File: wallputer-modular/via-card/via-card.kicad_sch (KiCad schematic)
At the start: 1 part

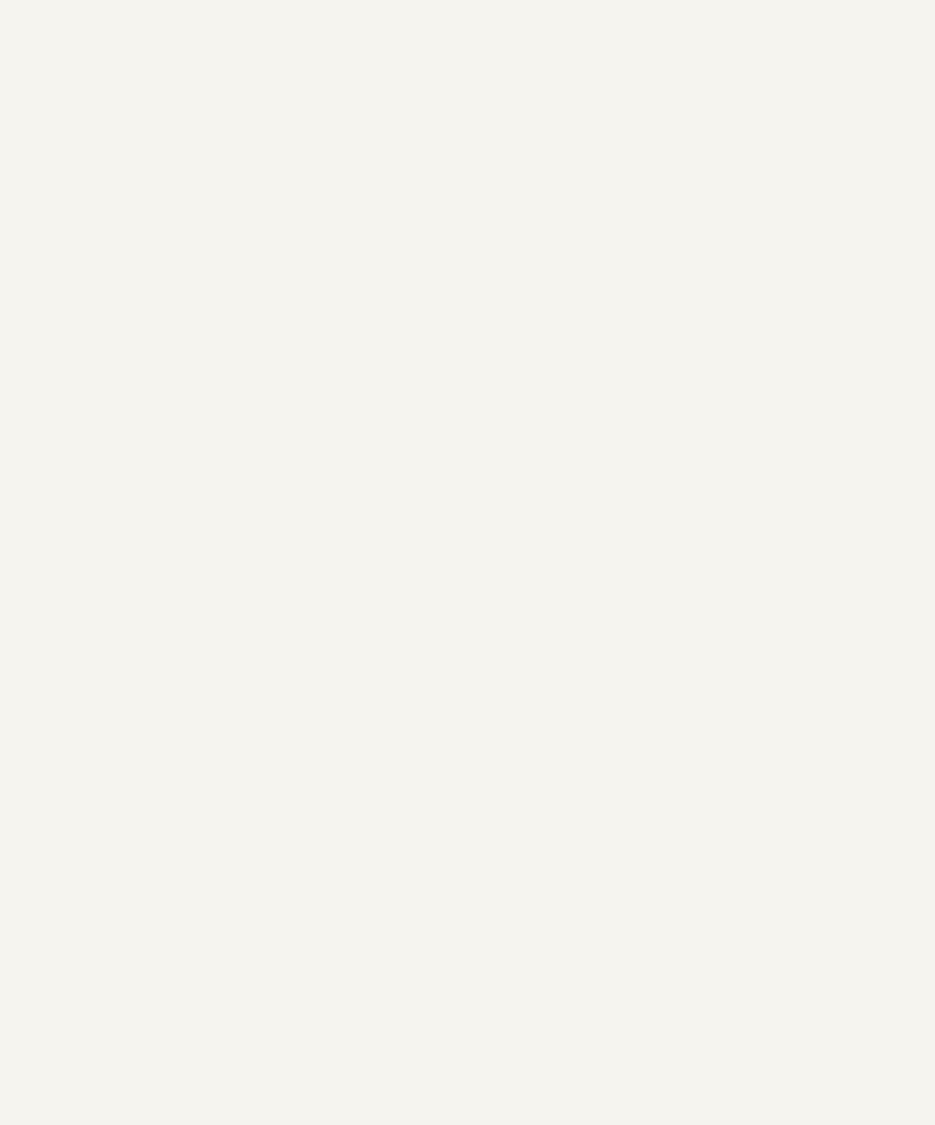
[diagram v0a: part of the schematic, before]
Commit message: copy parts of single board
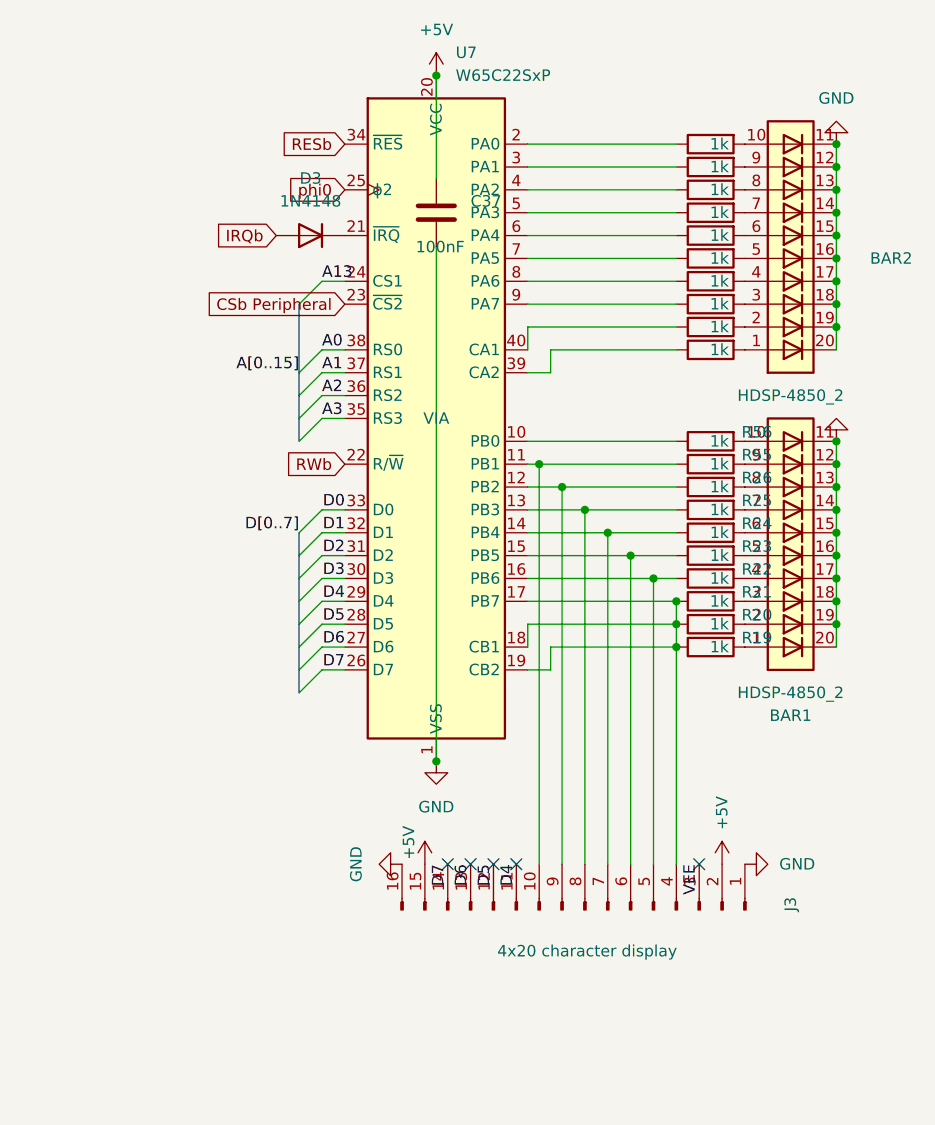
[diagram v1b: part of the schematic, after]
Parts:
- added BAR1, BAR2: HDSP-4850_2, Display:HDSP-4850, symbol LED:HDSP-4850_2
- added C37: 100nF, Capacitor_THT:C_Disc_D5.0mm_W2.5mm_P5.00mm, symbol Device:C
- added D3: 1N4148, Diode_THT:D_DO-35_SOD27_P7.62mm_Horizontal, symbol Diode:1N4148
- added J3: 4x20 character display, Connector_PinHeader_2.54mm:PinHeader_1x16_P2.54mm_Vertical, symbol Connector:Conn_01x16_Pin
- added R19, R20, R21, R22, R23, R24, R25, R26, R51, R52, R55, R56, R57, R58, R59, R60, R61, R62, R63, R64: 1k, Resistor_THT:R_Axial_DIN0204_L3.6mm_D1.6mm_P2.54mm_Vertical, symbol Device:R
- added U7: W65C22SxP, Package_DIP:DIP-40_W15.24mm, symbol 65xx-library:W65C22SxP
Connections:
- net +5V: now also C37.1, J3.15 (Pin_15), J3.2 (Pin_2), U7.20 (VCC)
- net GND: now also BAR1.11 (K), BAR1.12 (K), BAR1.13 (K), BAR1.14 (K), BAR1.15 (K), BAR1.16 (K), BAR1.17 (K), BAR1.18 (K), BAR1.19 (K), BAR1.20 (K), BAR2.11 (K), BAR2.12 (K), BAR2.13 (K), BAR2.14 (K), BAR2.15 (K), BAR2.16 (K), BAR2.17 (K), BAR2.18 (K), BAR2.19 (K), BAR2.20 (K), C37.2, J3.1 (Pin_1), J3.16 (Pin_16), U7.1 (VSS)
- new net: J3.6 (Pin_6), R23.1, U7.15 (PB5)
- new net: BAR1.5 (A), R23.2
- new net: R52.1, U7.3 (PA1)
- new net: BAR2.9 (A), R52.2
- new net: J3.4 (Pin_4), R19.1, R20.1, R21.1, U7.17 (PB7), U7.18 (CB1), U7.19 (CB2)
- new net: BAR1.2 (A), R20.2
- new net: R51.1, U7.2 (PA0)
- new net: BAR2.10 (A), R51.2
- new net: BAR2.1 (A), R59.2
- new net: BAR2.2 (A), R60.2
- new net: BAR2.3 (A), R61.2
- new net: BAR2.4 (A), R62.2
- new net: BAR2.5 (A), R63.2
- new net: BAR2.6 (A), R64.2
- new net: BAR2.7 (A), R58.2
- new net: BAR2.8 (A), R57.2
- new net: R60.1, U7.40 (CA1)
- new net: R63.1, U7.7 (PA5)
- new net: D3.1 (K), U7.21 (~{IRQ})
- new net: J3.9 (Pin_9), R26.1, U7.12 (PB2)
- new net: BAR1.8 (A), R26.2
- new net: J3.10 (Pin_10), R55.1, U7.11 (PB1)
- new net: BAR1.9 (A), R55.2
- new net: R57.1, U7.4 (PA2)
- new net: BAR1.1 (A), R19.2
- new net: R62.1, U7.8 (PA6)
- new net: BAR1.10 (A), R56.2
- new net: BAR1.3 (A), R21.2
- new net: BAR1.4 (A), R22.2
- new net: BAR1.6 (A), R24.2
- new net: BAR1.7 (A), R25.2
- new net: J3.5 (Pin_5), R22.1, U7.16 (PB6)
- new net: R59.1, U7.39 (CA2)
- new net: R61.1, U7.9 (PA7)
- new net: J3.7 (Pin_7), R24.1, U7.14 (PB4)
- new net: J3.8 (Pin_8), R25.1, U7.13 (PB3)
- new net: R64.1, U7.6 (PA4)
- new net: R56.1, U7.10 (PB0)
- new net: R58.1, U7.5 (PA3)
- new net A0: U7.38 (RS0)
- new net A1: U7.37 (RS1)
- new net A13: U7.24 (CS1)
- new net A2: U7.36 (RS2)
- new net A3: U7.35 (RS3)
- new net CSb Peripheral: U7.23 (~{CS2})
- new net D0: U7.33 (D0)
- new net D1: U7.32 (D1)
- new net D2: U7.31 (D2)
- new net D3: U7.30 (D3)
- new net D4: J3.11 (Pin_11), U7.29 (D4)
- new net D5: J3.12 (Pin_12), U7.28 (D5)
- new net D6: J3.13 (Pin_13), U7.27 (D6)
- new net D7: J3.14 (Pin_14), U7.26 (D7)
- new net IRQb: D3.2 (A)
- new net RESb: U7.34 (~{RES})
- new net RWb: U7.22 (R/~{W})
- new net VEE: J3.3 (Pin_3)
- new net phi0: U7.25 (ϕ2)
- no-connect marks 0 -> 5

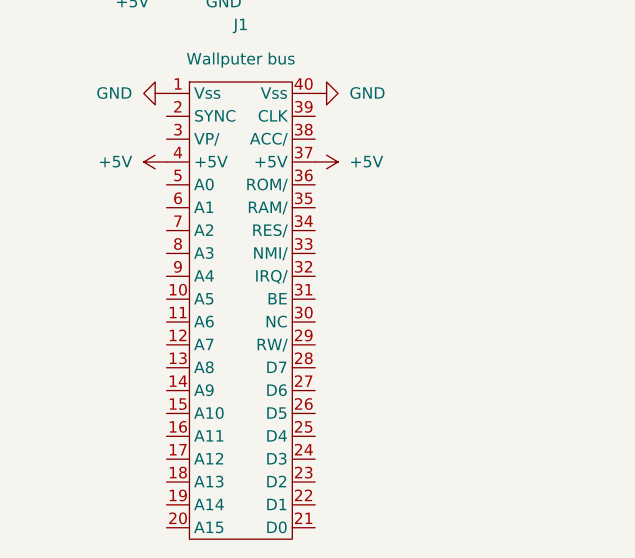
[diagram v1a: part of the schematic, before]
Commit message: implement acia card
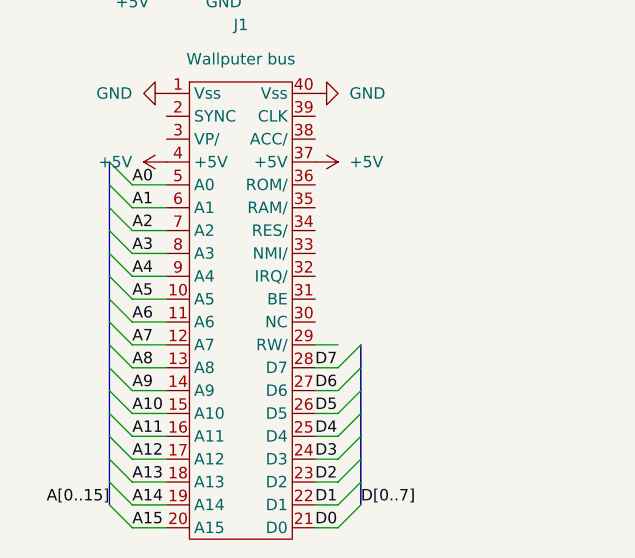
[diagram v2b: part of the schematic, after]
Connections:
- net A0: now also J1.5 (A0)
- net A1: now also J1.6 (A1)
- net A13: now also J1.18 (A13)
- net A2: now also J1.7 (A2)
- net A3: now also J1.8 (A3)
- net D0: now also J1.21 (D0)
- net D1: now also J1.22 (D1)
- net D2: now also J1.23 (D2)
- net D3: now also J1.24 (D3)
- net D4: now also J1.25 (D4)
- net D5: now also J1.26 (D5)
- net D6: now also J1.27 (D6)
- net D7: now also J1.28 (D7)
- net A5: now reaches J1.10 (A5)
- net A6: now reaches J1.11 (A6)
- net A7: now reaches J1.12 (A7)
- net A8: now reaches J1.13 (A8)
- net A9: now reaches J1.14 (A9)
- net A10: now reaches J1.15 (A10)
- net A11: now reaches J1.16 (A11)
- net A12: now reaches J1.17 (A12)
- net A14: now reaches J1.19 (A14)
- net A15: now reaches J1.20 (A15)
- net A4: now reaches J1.9 (A4)

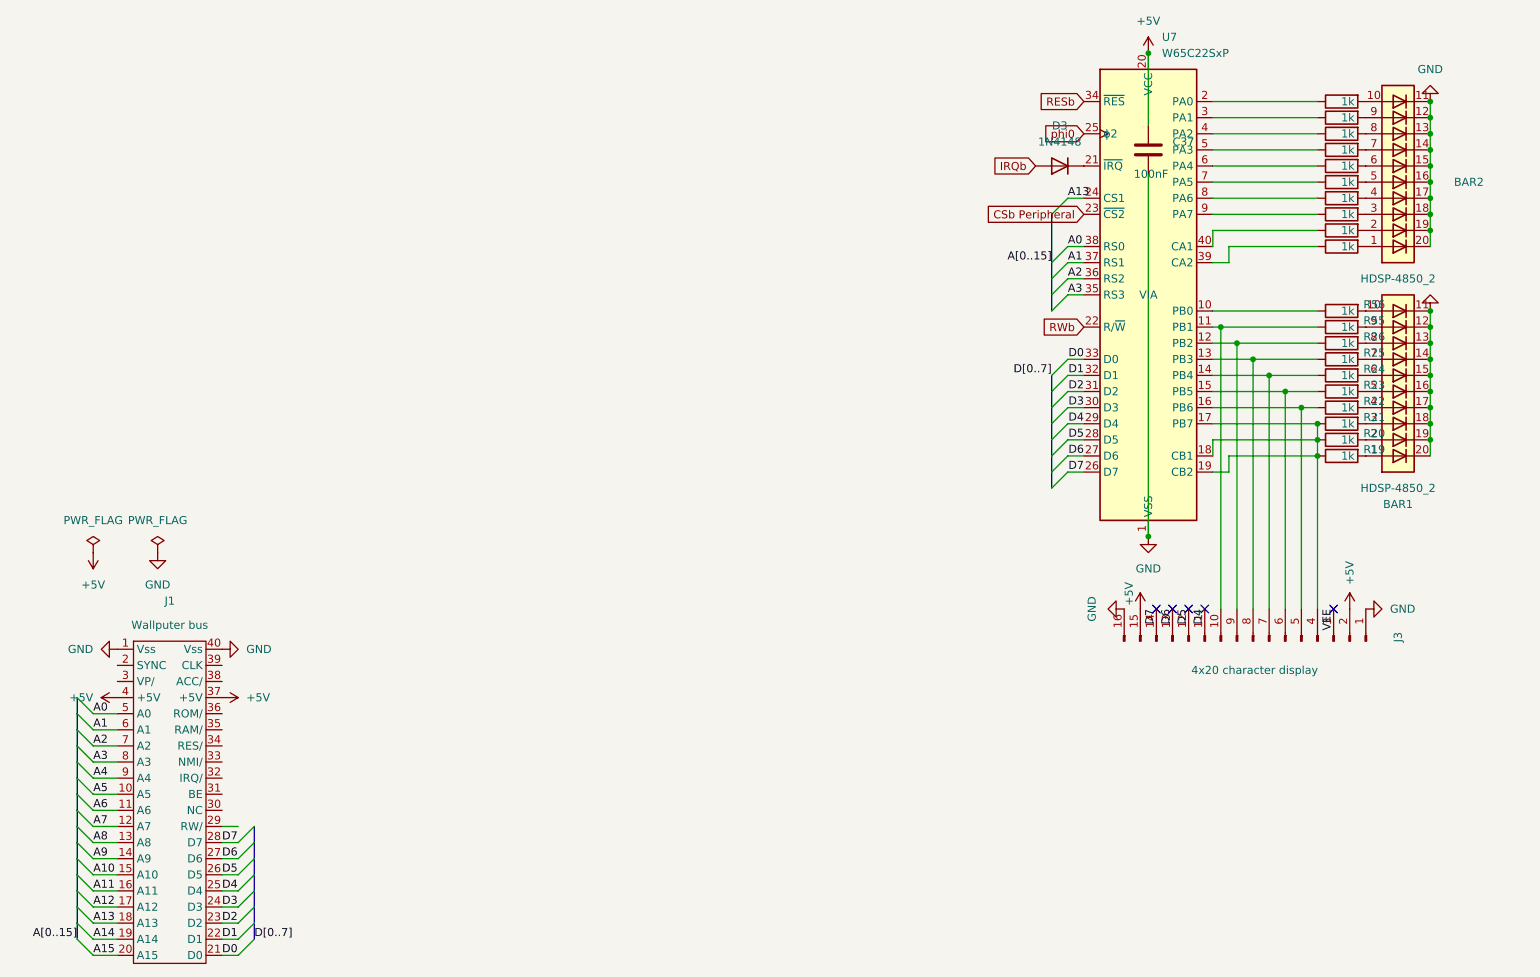
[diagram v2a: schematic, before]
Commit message: implement via board
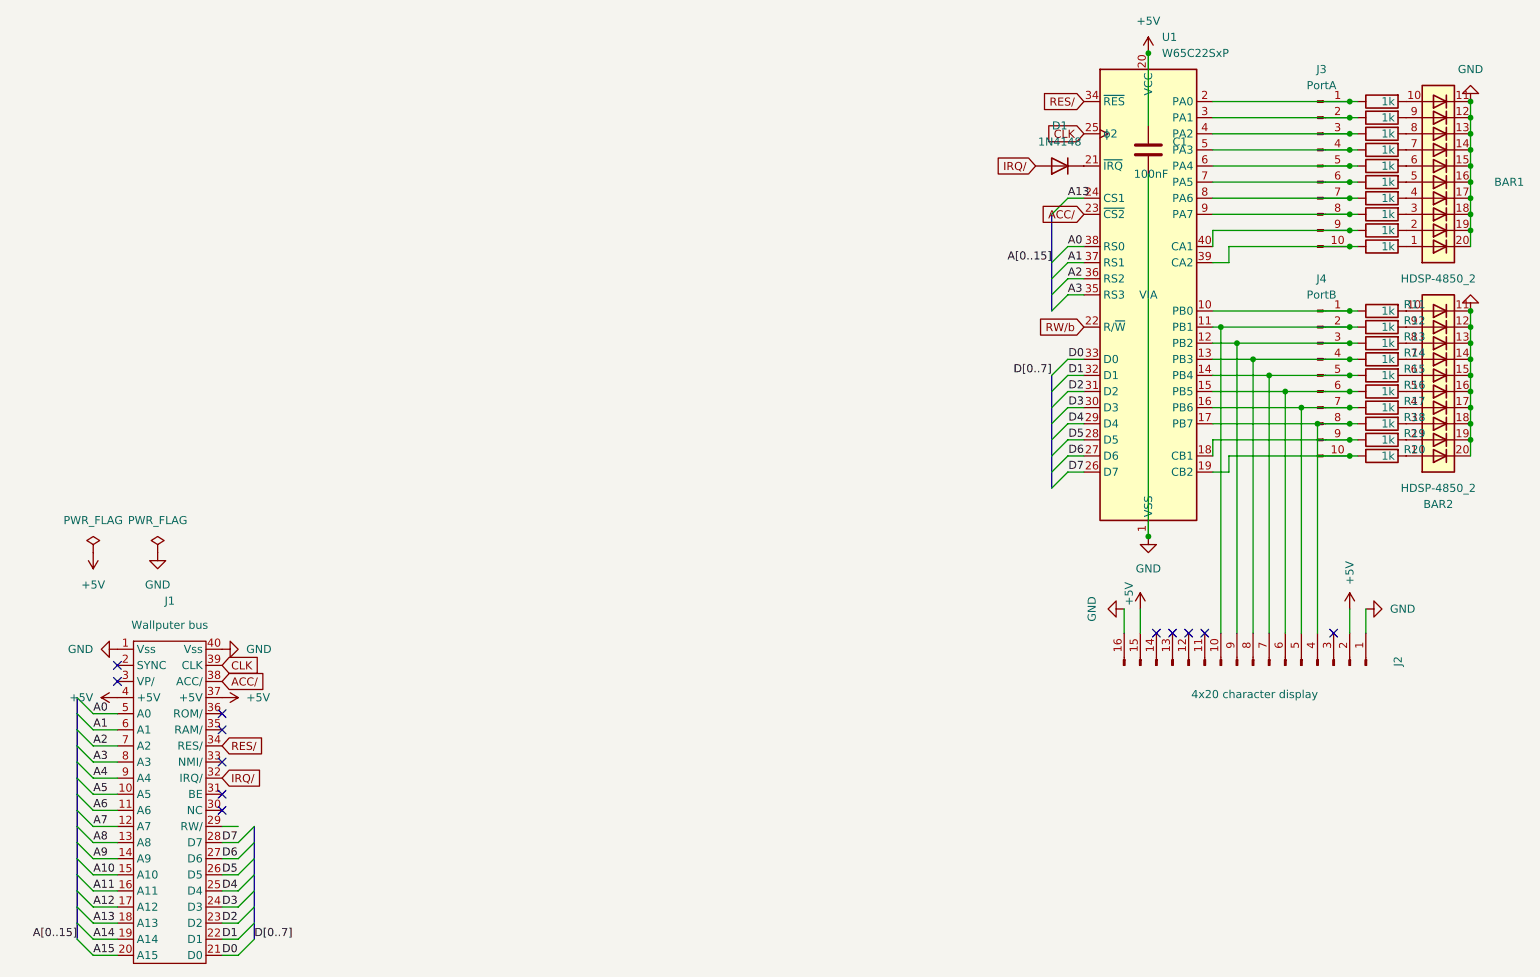
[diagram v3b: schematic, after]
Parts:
- added J3: PortA, Connector_PinHeader_2.54mm:PinHeader_1x10_P2.54mm_Vertical, symbol Connector:Conn_01x10_Pin
- added J4: PortB, Connector_PinHeader_2.54mm:PinHeader_1x10_P2.54mm_Vertical, symbol Connector:Conn_01x10_Pin
- renumbered BAR2 to BAR1, BAR1 to BAR2, C37 to C1, D3 to D1, J3 to J2, R51 to R1, R59 to R10, R56 to R11, R55 to R12, R26 to R13, R25 to R14, R24 to R15, R23 to R16, R22 to R17, R21 to R18, R20 to R19, R52 to R2, R19 to R20, R57 to R3, R58 to R4, R64 to R5, R63 to R6, R62 to R7, R61 to R8, R60 to R9, U7 to U1
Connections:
- net CSb Peripheral is gone; now on net ACC/: U1.23 (~{CS2})
- net IRQb is gone; now on net IRQ/: D1.2 (A)
- net RESb is gone; now on net RES/: U1.34 (~{RES})
- net phi0 is gone; now on net CLK: U1.25 (ϕ2)
- net D4: no longer J2.11 (Pin_11)
- net D5: no longer J2.12 (Pin_12)
- net D6: no longer J2.13 (Pin_13)
- net D7: no longer J2.14 (Pin_14)
- net at J2.6 (Pin_6), R16.1, U1.15 (PB5): now also J4.6 (Pin_6)
- net at R2.1, U1.3 (PA1): now also J3.2 (Pin_2)
- net IRQ/: now reaches J1.32 (IRQ/)
- net RES/: now reaches J1.34 (RES/)
- net ACC/: now reaches J1.38 (ACC/)
- net CLK: now reaches J1.39 (CLK)
- net at R1.1, U1.2 (PA0): now also J3.1 (Pin_1)
- net at R9.1, U1.40 (CA1): now also J3.9 (Pin_9)
- net at R6.1, U1.7 (PA5): now also J3.6 (Pin_6)
- net at J2.9 (Pin_9), R13.1, U1.12 (PB2): now also J4.3 (Pin_3)
- net at J2.10 (Pin_10), R12.1, U1.11 (PB1): now also J4.2 (Pin_2)
- net at R3.1, U1.4 (PA2): now also J3.3 (Pin_3)
- net at R7.1, U1.8 (PA6): now also J3.7 (Pin_7)
- net at J2.5 (Pin_5), R17.1, U1.16 (PB6): now also J4.7 (Pin_7)
- net at R10.1, U1.39 (CA2): now also J3.10 (Pin_10)
- net at R8.1, U1.9 (PA7): now also J3.8 (Pin_8)
- net at J2.7 (Pin_7), R15.1, U1.14 (PB4): now also J4.5 (Pin_5)
- net at J2.8 (Pin_8), R14.1, U1.13 (PB3): now also J4.4 (Pin_4)
- net at R5.1, U1.6 (PA4): now also J3.5 (Pin_5)
- net at R11.1, U1.10 (PB0): now also J4.1 (Pin_1)
- net at R4.1, U1.5 (PA3): now also J3.4 (Pin_4)
- net RWb renamed RW/b
- net VEE: no longer names the net of J2.3 (Pin_3)
- new net: J4.9 (Pin_9), R19.1, U1.18 (CB1)
- new net: J4.10 (Pin_10), R20.1, U1.19 (CB2)
- new net: J2.4 (Pin_4), J4.8 (Pin_8), R18.1, U1.17 (PB7)
- no-connect marks 5 -> 12
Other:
- moved on the sheet: BAR1, BAR2, J2, R11, R12, R13, R14, R15, R16, R17, R18, R19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
